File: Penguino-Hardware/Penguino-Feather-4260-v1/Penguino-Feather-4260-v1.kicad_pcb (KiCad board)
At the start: 4 copper layers, 22.9 x 50.8 mm, 60 parts, among them J1 U.FL-R-SMT-1, J2 SMA-Edge-Mount, J3 USB_C_Receptacle_USB2.0, J4 JST_PH, J5 Conn_ARM_JTAG_SWD_10, Q1 SI2323DS, SW1 USR_BTN, SW2 RESET, U1 MCP73831, U2 ME6215C33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

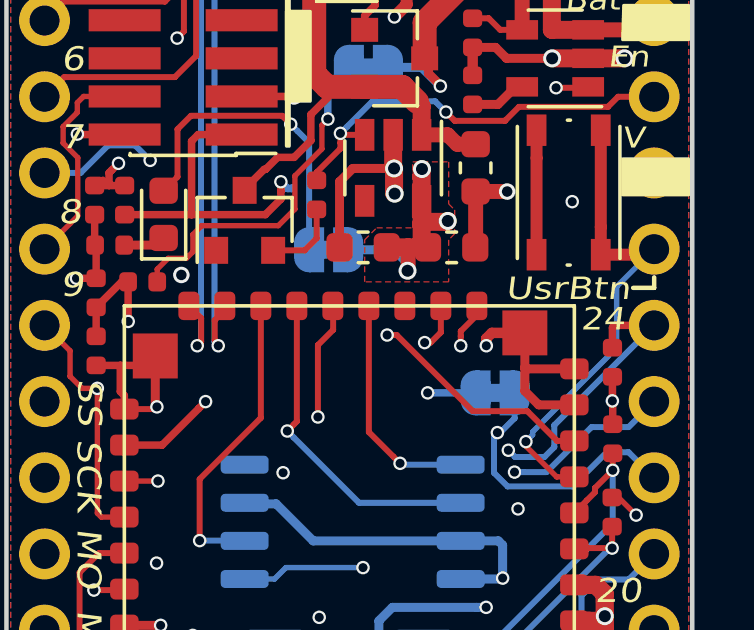
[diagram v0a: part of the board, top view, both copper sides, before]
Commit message: RAK4260 datasheet pin error
PA19 and PA18 are swapped
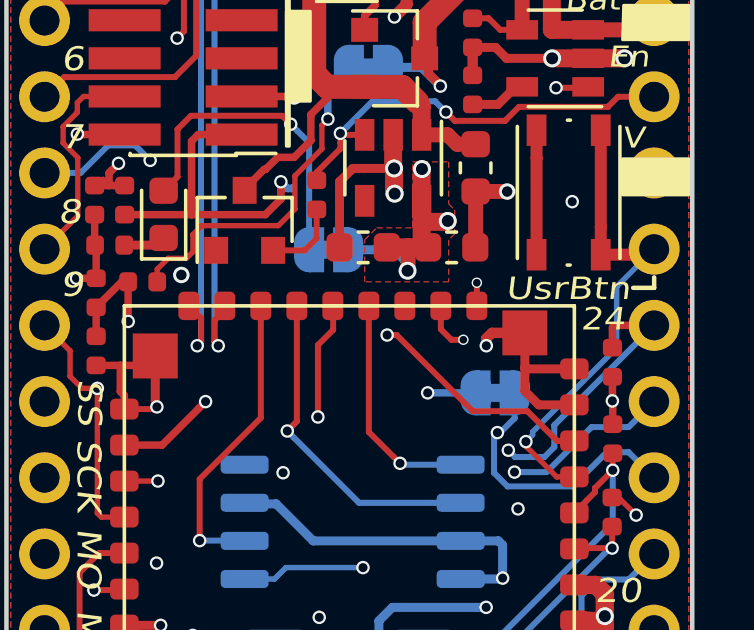
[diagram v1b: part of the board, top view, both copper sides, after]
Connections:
- U4 pad 19: PA18_TX3 -> PA19_RX3
- U4 pad 20: PA19_RX3 -> PA18_TX3
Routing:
- net PA19_RX3: track 35.0 -> 37.1 mm
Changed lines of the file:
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@@
     (thickness 1.6)
     (drawings 90)
-    (tracks 915)
+    (tracks 914)
     (zones 0)
     (modules 60)
@@
       (drillshape 0)
       (scaleselection 1)
-      (outputdirectory "fabrication/gerbers"))
+      (outputdirectory "fabrication/gerbers/"))
   )
   (net 0 "")
@@
       (net 54 "Net-(U4-Pad21)"))
     (pad 20 smd roundrect (at 7.5 3.05 270) (size 0.95 0.7) (layers Top.HF F.Paste F.Mask) (roundrect_rratio 0.25)
-      (net 15 PA19_RX3))
-    (pad 19 smd roundrect (at 7.5 4.25 270) (size 0.95 0.7) (layers Top.HF F.Paste F.Mask) (roundrect_rratio 0.25)
       (net 17 PA18_TX3))
+    (pad 19 smd roundrect (at 7.5 4.25 270) (size 0.95 0.7) (layers Top.HF F.Paste F.Mask) (roundrect_rratio 0.25)
+      (net 15 PA19_RX3))
     (pad 36 smd roundrect (at -5.54 -7.5 180) (size 0.95 0.7) (layers Top.HF F.Paste F.Mask) (roundrect_rratio 0.25)
       (net 1 GND))
@@
   (segment (start 129.25 89.75) (end 128.75 89.25) (width 0.2) (layer Bottom.LF) (net 15))
   (segment (start 128.75 89.25) (end 127.852081 89.25) (width 0.2) (layer Bottom.LF) (net 15))
-  (via (at 138.4 95.825) (size 0.45) (drill 0.3) (layers Top.HF Bottom.LF) (net 15))
-  (segment (start 138.94 95.485) (end 138.94 94.601) (width 0.2) (layer Top.HF) (net 15))
-  (segment (start 138.4 95.825) (end 138.6 95.825) (width 0.2) (layer Top.HF) (net 15))
-  (segment (start 138.6 95.825) (end 138.94 95.485) (width 0.2) (layer Top.HF) (net 15))
-  (segment (start 138.175001 96.049999) (end 138.4 95.825) (width 0.2) (layer In2.PWR) (net 15))
+  (segment (start 140.14 94.601) (end 140.14 94.91) (width 0.2) (layer Top.HF) (net 15))
+  (via (at 140.14 93.83) (size 0.35) (drill 0.254) (layers Top.HF Bottom.LF) (net 15))
+  (segment (start 140.14 94.601) (end 140.14 93.83) (width 0.2) (layer Top.HF) (net 15))
+  (segment (start 137.672513 96.05) (end 139.892513 93.83) (width 0.2) (layer In2.PWR) (net 15))
   (segment (start 129.25 89.75) (end 129.25 93.99) (width 0.2) (layer In2.PWR) (net 15))
-  (segment (start 132.156616 95.23) (end 132.976616 96.05) (width 0.2) (layer In2.PWR) (net 15))
-  (segment (start 129.25 93.99) (end 130.49 95.23) (width 0.2) (layer In2.PWR) (net 15))
+  (segment (start 139.892513 93.83) (end 140.14 93.83) (width 0.2) (layer In2.PWR) (net 15))
   (segment (start 130.49 95.23) (end 132.156616 95.23) (width 0.2) (layer In2.PWR) (net 15))
-  (segment (start 132.976616 96.05) (end 138.175001 96.049999) (width 0.2) (layer In2.PWR) (net 15))
+  (segment (start 129.25 93.99) (end 130.49 95.23) (width 0.2) (layer In2.PWR) (net 15))
+  (segment (start 132.976616 96.05) (end 137.672513 96.05) (width 0.2) (layer In2.PWR) (net 15))
+  (segment (start 132.156616 95.23) (end 132.976616 96.05) (width 0.2) (layer In2.PWR) (net 15))
   (segment (start 143.804844 101.086156) (end 143.39 101.501) (width 0.2) (layer Top.HF) (net 16))
   (segment (start 144.07759 100.81341) (end 143.804844 101.086156) (width 0.2) (layer Top.HF) (net 16))
@@
   (segment (start 139.93 107.53) (end 139.6 107.2) (width 0.2) (layer In2.PWR) (net 16))
   (segment (start 139.6 106.3) (end 140.125 105.775) (width 0.2) (layer In2.PWR) (net 16))
-  (via (at 139.603285 95.930009) (size 0.45) (drill 0.3) (layers Top.HF Bottom.LF) (net 17))
   (segment (start 130.075 86.975) (end 126.385 86.975) (width 0.2) (layer Top.HF) (net 17))
   (segment (start 126.385 86.975) (end 125.73 87.63) (width 0.2) (layer Top.HF) (net 17))
@@
   (segment (start 130.782812 71.877812) (end 130.782812 86.267188) (width 0.2) (layer Top.HF) (net 17))
   (segment (start 129.921 71.016) (end 130.782812 71.877812) (width 0.2) (layer Top.HF) (net 17))
-  (segment (start 139.603285 95.611811) (end 139.603285 95.930009) (width 0.2) (layer Top.HF) (net 17))
-  (segment (start 139.603285 95.446715) (end 139.603285 95.611811) (width 0.2) (layer Top.HF) (net 17))
-  (segment (start 140.14 94.601) (end 140.14 94.91) (width 0.2) (layer Top.HF) (net 17))
-  (segment (start 140.14 94.91) (end 139.603285 95.446715) (width 0.2) (layer Top.HF) (net 17))
-  (segment (start 138.84 98.16) (end 139.603285 97.396715) (width 0.18) (layer In2.PWR) (net 17))
-  (segment (start 138.028446 98.16) (end 138.84 98.16) (width 0.18) (layer In2.PWR) (net 17))
-  (segment (start 137.618446 97.75) (end 138.028446 98.16) (width 0.18) (layer In2.PWR) (net 17))
-  (segment (start 139.603285 97.396715) (end 139.603285 95.930009) (width 0.18) (layer In2.PWR) (net 17))
-  (segment (start 127.639822 94.372884) (end 127.639822 96.502224) (width 0.18) (layer In2.PWR) (net 17))
-  (segment (start 127.717411 94.295295) (end 127.639822 94.372884) (width 0.18) (layer In2.PWR) (net 17))
-  (segment (start 125.73 87.63) (end 126.932081 87.63) (width 0.18) (layer In2.PWR) (net 17))
-  (segment (start 127.717411 88.41533) (end 127.717411 94.295295) (width 0.18) (layer In2.PWR) (net 17))
-  (segment (start 132.29 97.75) (end 137.618446 97.75) (width 0.18) (layer In2.PWR) (net 17))
-  (segment (start 127.639822 96.502224) (end 128.068799 96.931201) (width 0.18) (layer In2.PWR) (net 17))
-  (segment (start 128.068799 96.931201) (end 128.068799 98.108799) (width 0.18) (layer In2.PWR) (net 17))
-  (segment (start 128.068799 98.108799) (end 128.56 98.6) (width 0.18) (layer In2.PWR) (net 17))
-  (segment (start 126.932081 87.63) (end 127.717411 88.41533) (width 0.18) (layer In2.PWR) (net 17))
-  (segment (start 128.56 98.6) (end 131.44 98.6) (width 0.18) (layer In2.PWR) (net 17))
-  (segment (start 131.44 98.6) (end 132.29 97.75) (width 0.18) (layer In2.PWR) (net 17))
+  (via (at 139.69 95.73) (size 0.35) (drill 0.254) (layers Top.HF Bottom.LF) (net 17))
+  (segment (start 138.94 95.38) (end 138.94 94.601) (width 0.2) (layer Top.HF) (net 17))
+  (segment (start 139.69 95.73) (end 139.29 95.73) (width 0.2) (layer Top.HF) (net 17))
+  (segment (start 139.29 95.73) (end 138.94 95.38) (width 0.2) (layer Top.HF) (net 17))
+  (segment (start 126.932081 87.63) (end 125.73 87.63) (width 0.18) (layer In2.PWR) (net 17))
+  (segment (start 127.717411 88.41533) (end 126.932081 87.63) (width 0.18) (layer In2.PWR) (net 17))
+  (segment (start 127.717411 94.295295) (end 127.717411 88.41533) (width 0.18) (layer In2.PWR) (net 17))
+  (segment (start 127.639822 94.372884) (end 127.717411 94.295295) (width 0.18) (layer In2.PWR) (net 17))
+  (segment (start 138.028446 98.16) (end 137.618446 97.75) (width 0.18) (layer In2.PWR) (net 17))
+  (segment (start 137.618446 97.75) (end 132.29 97.75) (width 0.18) (layer In2.PWR) (net 17))
+  (segment (start 138.84 98.16) (end 138.028446 98.16) (width 0.18) (layer In2.PWR) (net 17))
+  (segment (start 139.69 95.73) (end 139.69 97.31) (width 0.18) (layer In2.PWR) (net 17))
+  (segment (start 131.44 98.6) (end 128.56 98.6) (width 0.18) (layer In2.PWR) (net 17))
+  (segment (start 132.29 97.75) (end 131.44 98.6) (width 0.18) (layer In2.PWR) (net 17))
+  (segment (start 128.56 98.6) (end 128.068799 98.108799) (width 0.18) (layer In2.PWR) (net 17))
+  (segment (start 139.69 97.31) (end 138.84 98.16) (width 0.18) (layer In2.PWR) (net 17))
+  (segment (start 128.068799 96.931201) (end 127.639822 96.502224) (width 0.18) (layer In2.PWR) (net 17))
+  (segment (start 128.068799 98.108799) (end 128.068799 96.931201) (width 0.18) (layer In2.PWR) (net 17))
+  (segment (start 127.639822 96.502224) (end 127.639822 94.372884) (width 0.18) (layer In2.PWR) (net 17))
   (via (at 144.65 102.675) (size 0.45) (drill 0.3) (layers Top.HF Bottom.LF) (net 18))
   (segment (start 144.65 101.96) (end 144.65 102.675) (width 0.2) (layer Top.HF) (net 18))
@@
       (pts
         (xy 130.8 94) (xy 130.8 91.6) (xy 130.8 87.4) (xy 130.8 78.8) (xy 124.8 78.8)
-        (xy 124.8 76.2) (xy 133.75 76.2) (xy 133.8 83.8) (xy 138 83.8) (xy 138 89.5)
-        (xy 140 89.5) (xy 140 92) (xy 144.25 92) (xy 144.25 103.5) (xy 144.75 103.5)
-        (xy 144.75 106) (xy 144.5 106) (xy 142.5 106) (xy 142.5 94)
+        (xy 124.8 76.2) (xy 134.815 76.2) (xy 134.815 83.8) (xy 138 83.8) (xy 139.765 83.78)
+        (xy 139.765 86.205) (xy 139.765 89.48) (xy 141.19 89.48) (xy 144.069451 92.685771) (xy 144.25 103.5)
+        (xy 144.75 103.5) (xy 144.75 106) (xy 144.5 106) (xy 142.5 106) (xy 142.5 94)
       )
     )
